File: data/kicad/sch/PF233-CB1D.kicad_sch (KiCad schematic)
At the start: 62 parts, among them M5 5 V 1.5 A switching module, U1 Pico 2 W

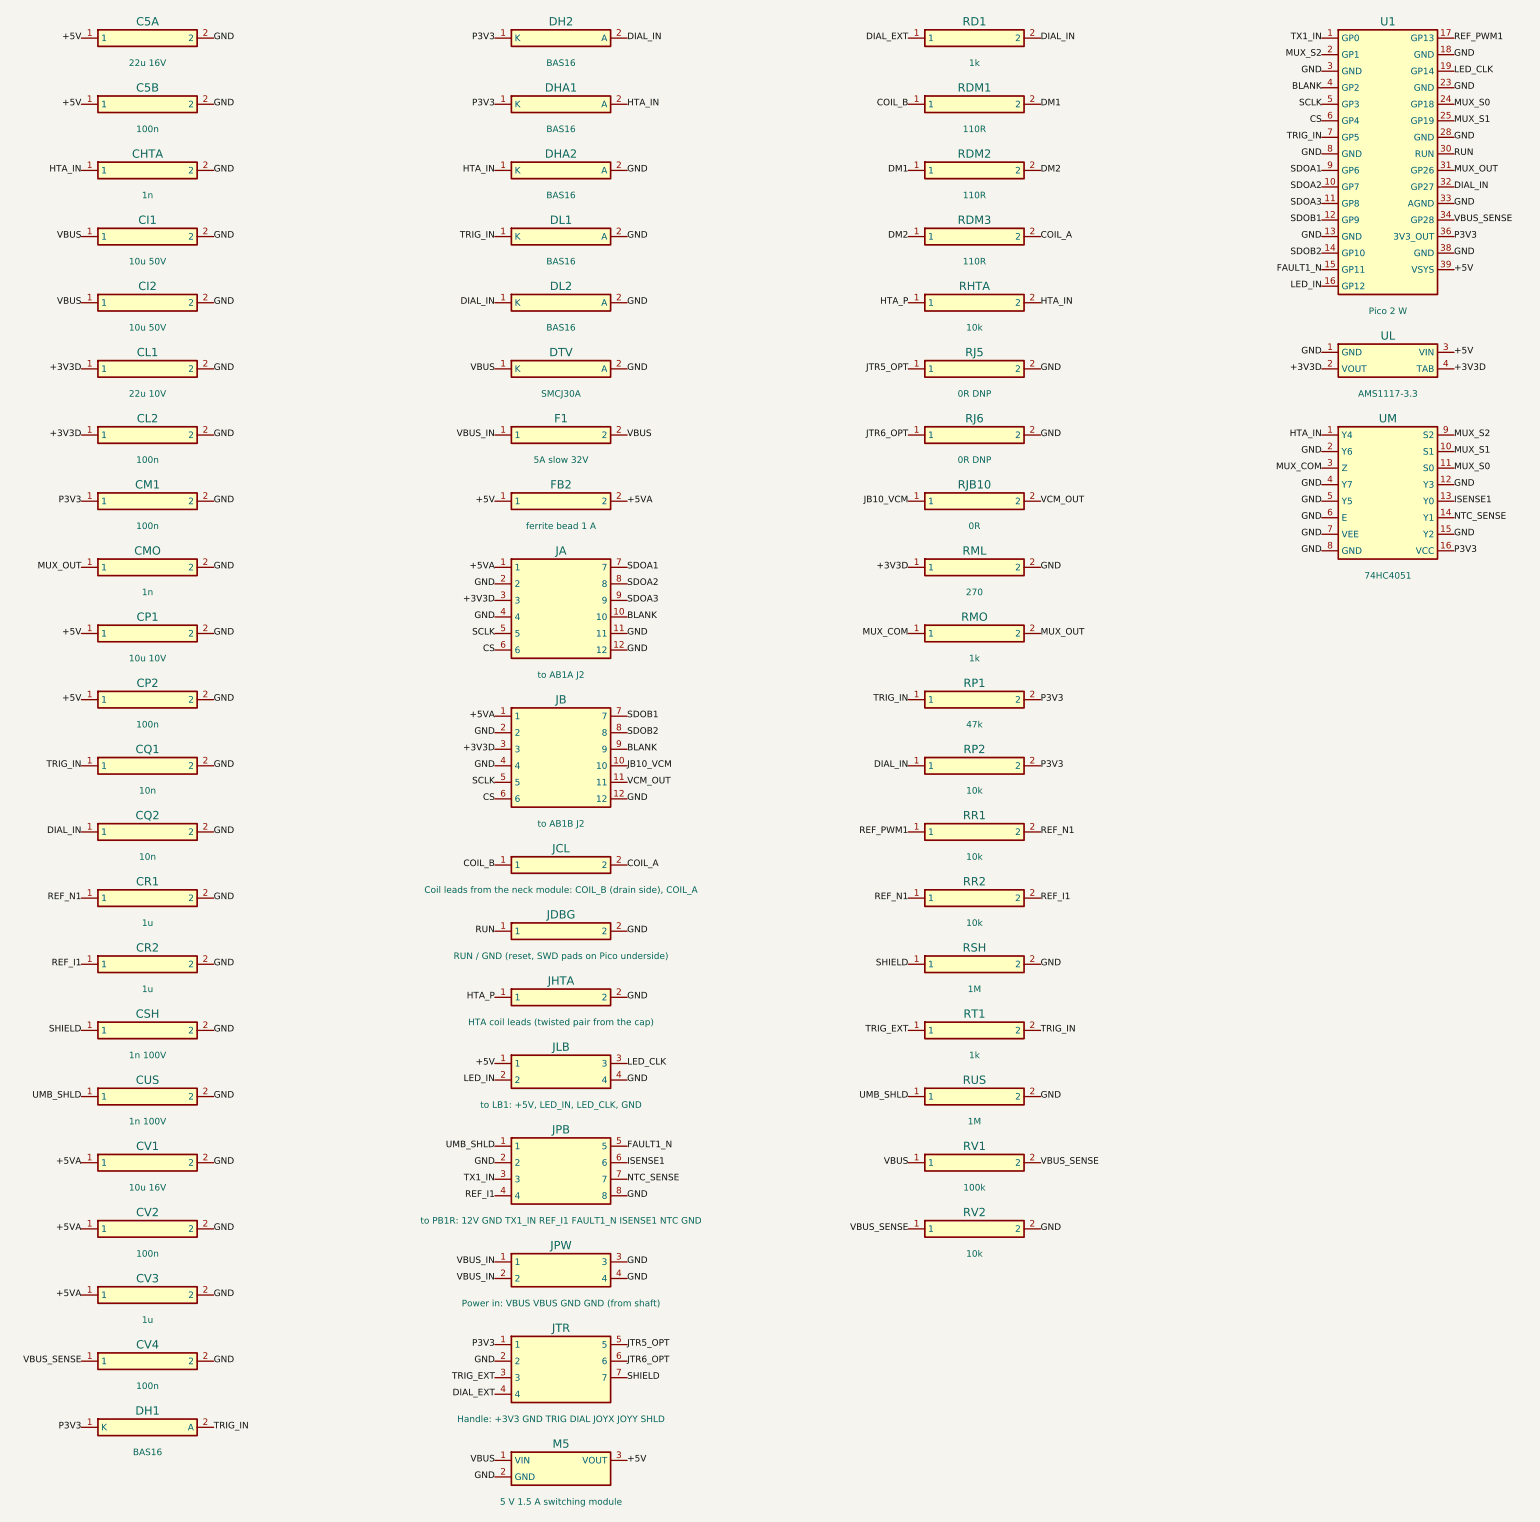
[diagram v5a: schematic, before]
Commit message: WIP: CB1D-C2 dual-source gyro land (BMI270 / LSM6DSO, pins 2-3 to VDDIO), LSM6DSO datasheet logged, gyro cluster re-placed for escape; CB1D re-route running
Co-Authored-By: Claude Opus 5.5 <noreply@anthropic.com>
Claude-Session: https://claude.ai/code/session_01FX4DWSYYjMCFGGA6gmha65
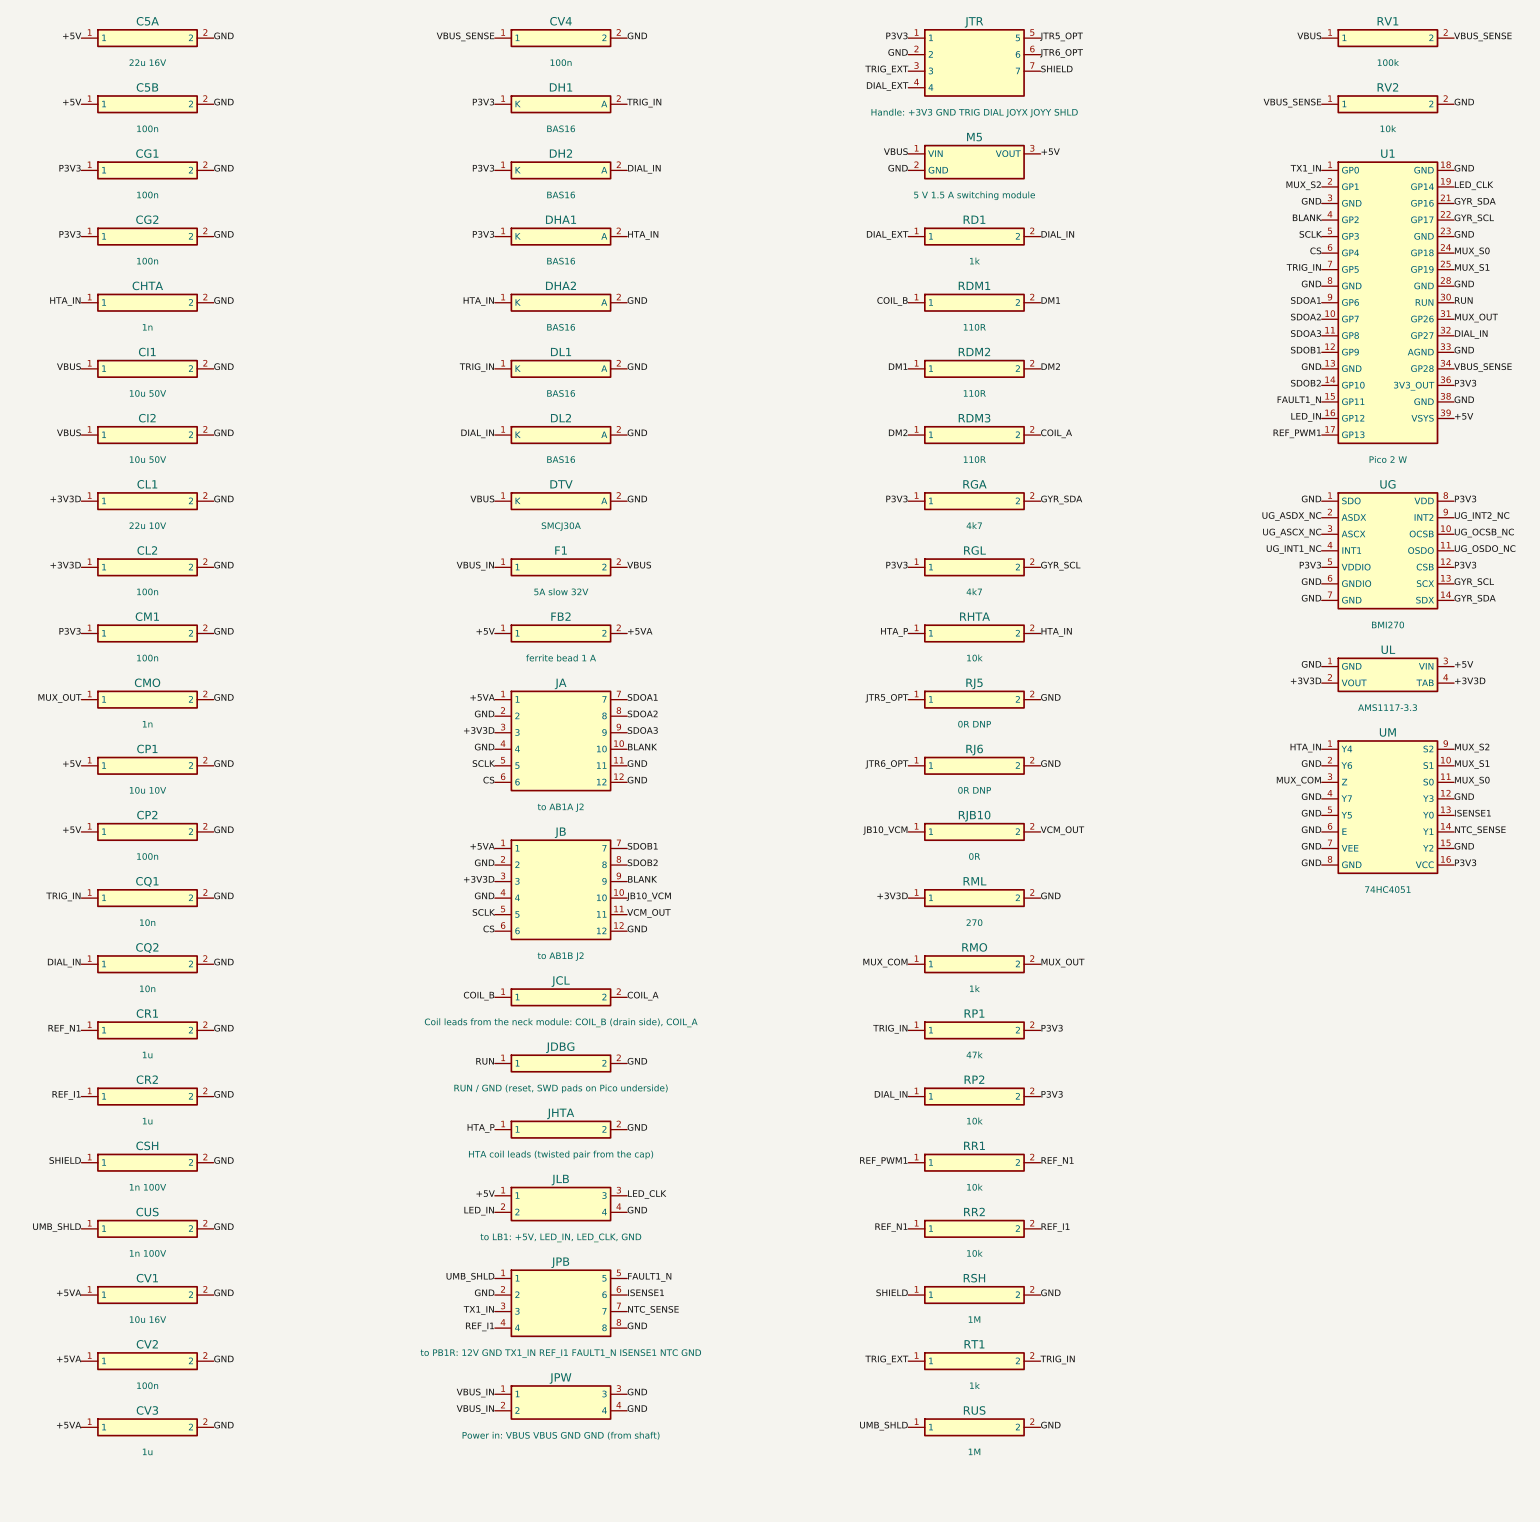
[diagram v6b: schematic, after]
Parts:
- added CG1: 100n, Capacitor_SMD:C_0603_1608Metric, symbol PF233_auto:CG1
- added CG2: 100n, Capacitor_SMD:C_0603_1608Metric, symbol PF233_auto:CG2
- added RGA: 4k7, Resistor_SMD:R_0603_1608Metric, symbol PF233_auto:RGA
- added RGL: 4k7, Resistor_SMD:R_0603_1608Metric, symbol PF233_auto:RGL
- added UG: BMI270, PF233:BMI270_LGA-14_2.5x3.0mm, symbol PF233_auto:UG
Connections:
- net GND: now also CG1.2, CG2.2, UG.1 (SDO), UG.6 (GNDIO), UG.7 (GND)
- net P3V3: now also CG1.1, CG2.1, RGA.1, RGL.1, UG.12 (CSB), UG.5 (VDDIO), UG.8 (VDD)
- new net GYR_SCL: RGL.2, U1.22 (GP17), UG.13 (SCX)
- new net GYR_SDA: RGA.2, U1.21 (GP16), UG.14 (SDX)
- new net UG_ASCX_NC: UG.3 (ASCX)
- new net UG_ASDX_NC: UG.2 (ASDX)
- new net UG_INT1_NC: UG.4 (INT1)
- new net UG_INT2_NC: UG.9 (INT2)
- new net UG_OCSB_NC: UG.10 (OCSB)
- new net UG_OSDO_NC: UG.11 (OSDO)
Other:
- moved on the sheet: CHTA, CI1, CI2, CL1, CL2, CM1, CMO, CP1, CP2, CQ1, CQ2, CR1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

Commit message: WIP (NOT signed off): data published by the first close-out sign-off run, which had 5 FAIL (CB1D-C2 / AU1 fine-pitch clearance); superseded by the rerun in progress
Co-Authored-By: Claude Opus 5.5 <noreply@anthropic.com>
Claude-Session: https://claude.ai/code/session_01FX4DWSYYjMCFGGA6gmha65
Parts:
- removed RJ5: 0R DNP, Resistor_SMD:R_0603_1608Metric, symbol PF233_auto:RJ5
- added DAU1: BAS16, Diode_SMD:D_SOD-123, symbol PF233_auto:DAU1
- added DAU2: BAS16, Diode_SMD:D_SOD-123, symbol PF233_auto:DAU2
- added RAU: 100R, Resistor_SMD:R_0603_1608Metric, symbol PF233_auto:RAU
- added RGF: 10R, Resistor_SMD:R_0603_1608Metric, symbol PF233_auto:RGF
- JTR: value Handle: +3V3 GND TRIG DIAL JOYX JOYY SHLD -> Handle: +3V3 GND TRIG DIAL AUD_LINK - SHLD
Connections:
- net UG_ASDX_NC is gone; now on net UG_VIO: UG.2 (ASDX)
- net GND: now also DAU2.2 (A); no longer UG.1 (SDO)
- net GYR_SCL: now also U1.27 (GP21); no longer U1.22 (GP17)
- net GYR_SDA: now also U1.26 (GP20); no longer U1.21 (GP16)
- net P3V3: now also DAU1.1 (K), RGF.1; no longer CG1.1, CG2.1, UG.12 (CSB), UG.5 (VDDIO), UG.8 (VDD)
- net JTR5_OPT renamed AUD_LINK
- net AUD_LINK: now also DAU1.2 (A), DAU2.1 (K), RAU.1
- net UG_ASCX_NC renamed UG_VIO
- net UG_VIO: now also CG1.1, CG2.1, UG.1 (SDO), UG.12 (CSB), UG.5 (VDDIO), UG.8 (VDD), RGF.2
- new net AUD_PIO: RAU.2, U1.20 (GP15)
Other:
- moved on the sheet: DH1, DH2, DHA1, DHA2, DL1, DL2, DTV, F1, FB2, JA, JB, JCL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

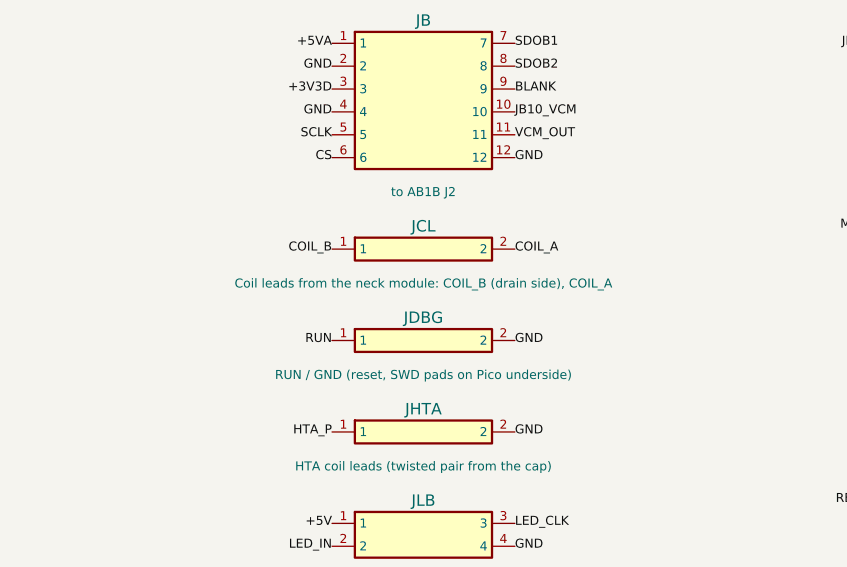
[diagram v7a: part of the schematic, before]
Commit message: WIP (NOT signed off): data published by the second close-out run (8 FAIL: 3 opens on CB1D-C2 / AU1 under the exact fine-zone keep-out); third run in progress
Co-Authored-By: Claude Opus 5.5 <noreply@anthropic.com>
Claude-Session: https://claude.ai/code/session_01FX4DWSYYjMCFGGA6gmha65
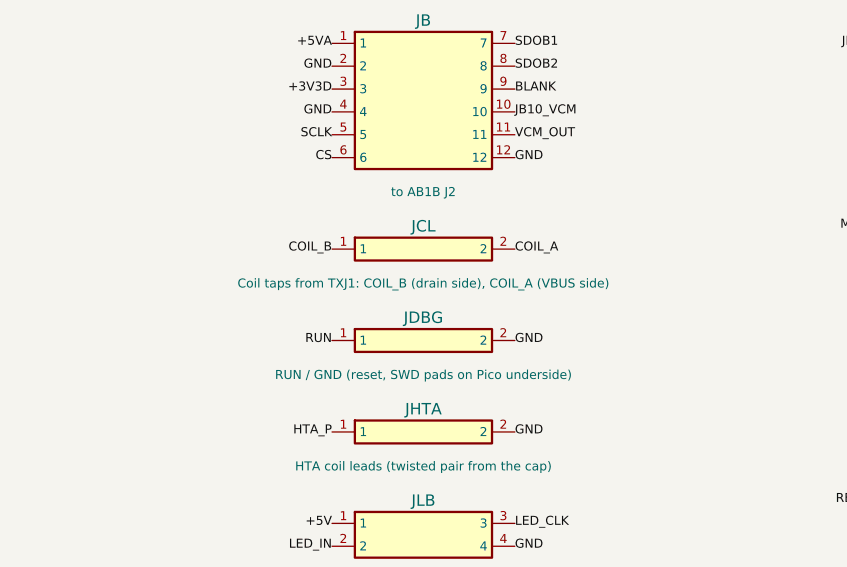
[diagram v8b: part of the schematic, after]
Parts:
- JCL: value Coil leads from the neck module: COIL_B (drain side), COIL_A -> Coil taps from TXJ1: COIL_B (drain side), COIL_A (VBUS side); footprint Connector:Terminal_block_1x2_P5.08mm -> Connector:Solder_holes_AWG22_1x2_P5.08mm
- JLB: footprint Connector:Pin_header_1x4_P2.54mm -> Connector:Wire_pads_1x4_P2.54mm
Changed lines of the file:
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@@
   (symbol (lib_id "PF233_auto:JCL") (at 93.98 198.12 0) (unit 1) (exclude_from_sim no) (in_bom yes) (on_board yes) (dnp no)
     (property "Reference" "JCL" (at 93.98 195.58 0) (effects (font (size 1.27 1.27))))
-    (property "Value" "Coil leads from the neck module: COIL_B (drain side), COIL_A" (at 93.98 201.93 0) (effects (font (size 1.0 1.0))))
-    (property "Footprint" "Connector:Terminal_block_1x2_P5.08mm" (at 93.98 198.12 0) (effects (font (size 1.27 1.27)) hide))
+    (property "Value" "Coil taps from TXJ1: COIL_B (drain side), COIL_A (VBUS side)" (at 93.98 201.93 0) (effects (font (size 1.0 1.0))))
+    (property "Footprint" "Connector:Solder_holes_AWG22_1x2_P5.08mm" (at 93.98 198.12 0) (effects (font (size 1.27 1.27)) hide))
     (pin "1")
     (pin "2")
@@
     (property "Reference" "JLB" (at 93.98 226.06 0) (effects (font (size 1.27 1.27))))
     (property "Value" "to LB1: +5V, LED_IN, LED_CLK, GND" (at 93.98 234.95 0) (effects (font (size 1.0 1.0))))
-    (property "Footprint" "Connector:Pin_header_1x4_P2.54mm" (at 93.98 228.60 0) (effects (font (size 1.27 1.27)) hide))
+    (property "Footprint" "Connector:Wire_pads_1x4_P2.54mm" (at 93.98 228.60 0) (effects (font (size 1.27 1.27)) hide))
     (pin "1")
     (pin "2")
